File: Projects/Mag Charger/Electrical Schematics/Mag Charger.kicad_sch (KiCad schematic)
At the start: 8 parts, among them J1 Conn_01x08, P1 USB_C_Plug_USB2.0

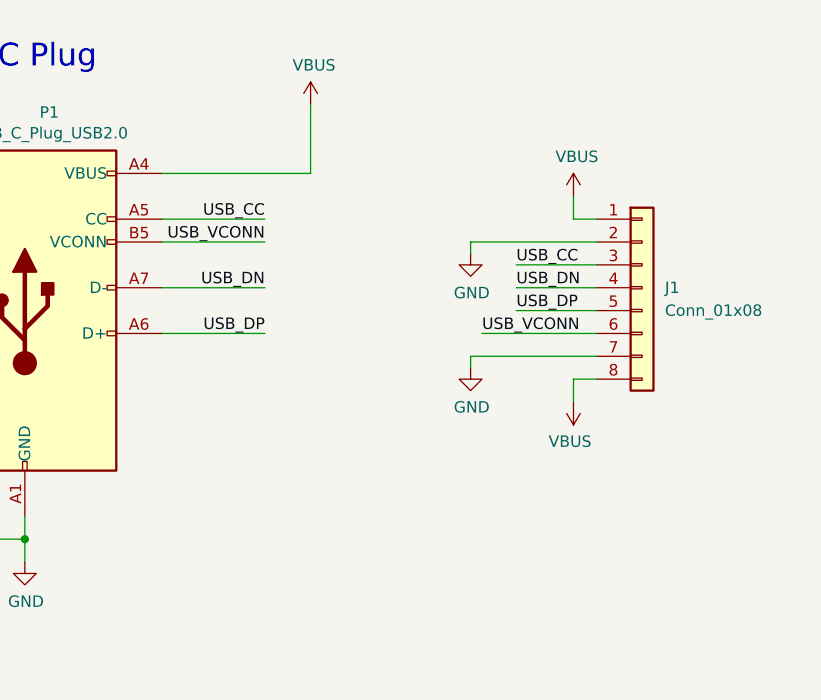
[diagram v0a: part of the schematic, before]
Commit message: Added ESD to mag charger schematic
Also worked on preliminary PCB layout.
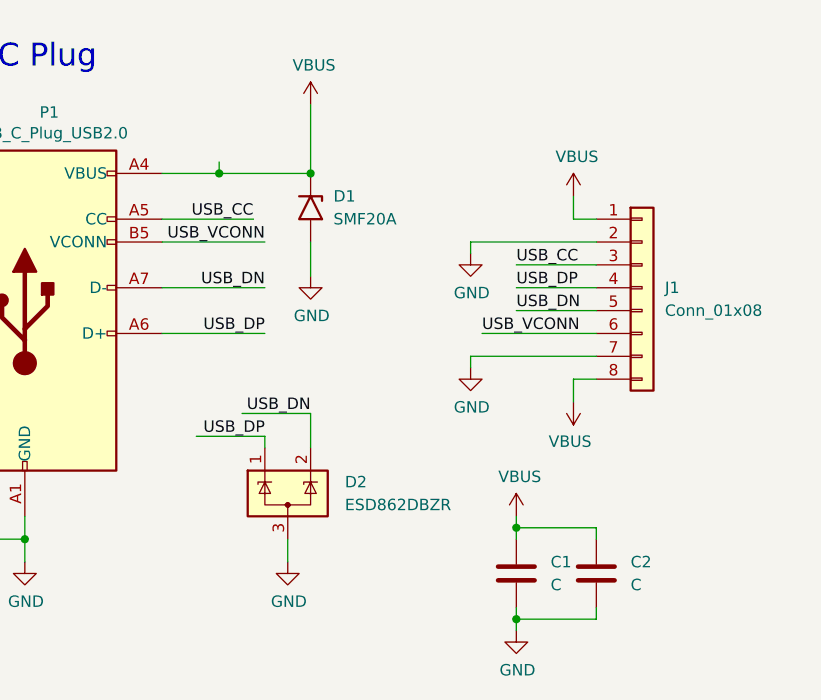
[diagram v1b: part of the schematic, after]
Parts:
- added C1, C2: C, Capacitor_SMD:C_1206_3216Metric_Pad1.33x1.80mm_HandSolder, symbol Device:C
- added D1: SMF20A, Diode_SMD:D_SMF, symbol Diode:SMF20A
- added D2: ESD862DBZR, SOT-23_Handsoldering, symbol Mag_Charger:ESD862DBZR
- J1: footprint (none) -> Mag Charger:Mag Connector
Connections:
- net GND: now also C1.2, C2.2, D1.2 (A2), D2.3 (A)
- net USB_DN: now also J1.5 (Pin_5), D2.2 (K); no longer J1.4 (Pin_4)
- net USB_DP: now also J1.4 (Pin_4), D2.1 (K); no longer J1.5 (Pin_5)
- net VBUS: now also C1.1, C2.1, D1.1 (A1)

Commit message: Finalized I2C Card
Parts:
- D1: value SMF20A -> SMBJ51ACT-ND; footprint Diode_SMD:D_SMF -> D_SMB_Handsoldering
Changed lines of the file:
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@@
 			)
 		)
-		(property "Value" "SMF20A"
+		(property "Value" "SMBJ51ACT-ND"
 			(at 76.2 43.1799 90)
 			(effects
@@
 			)
 		)
-		(property "Footprint" "Diode_SMD:D_SMF"
+		(property "Footprint" "D_SMB_Handsoldering"
 			(at 68.58 41.91 0)
 			(effects
@@
 			)
 		)
-		(property "Datasheet" "https://www.vishay.com/doc?85881"
+		(property "Datasheet" "https://www.diodes.com/assets/Datasheets/ds19002.pdf"
 			(at 73.66 40.64 0)
 			(effects
@@
 			)
 		)
-		(property "Description" "200W unidirectional Transil Transient Voltage Suppressor, 20Vrwm, SMF"
+		(property "Description" "TVS DIODE 51VWM 82.4VC DO214AA"
 			(at 73.66 41.91 0)
 			(effects
